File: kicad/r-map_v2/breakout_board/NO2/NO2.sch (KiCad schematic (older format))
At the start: 9 parts

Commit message: Update of schematic and new modules
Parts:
- removed P?: CONN_01X04, symbol CONN_01X04
- removed U?: MICS-2714, symbol MICS-2714
- added C2: 10n, Capacitors_SMD:C_0805_HandSoldering, symbol C
- added C?: C, symbol C
- added P1: CONN_01X08, Pin_Headers:Pin_Header_Straight_1x08_Pitch2.54mm, symbol CONN_01X08
- added P2: CONN_01X02, Pin_Headers:Pin_Header_Straight_1x02_Pitch2.54mm, symbol CONN_01X02
- added Q2: 2N7002, TO_SOT_Packages_SMD:SOT-23, symbol 2N7002
- added R10, R11: R, Resistors_SMD:R_0805, symbol R
- added R6: 330, Resistors_SMD:R_0805, symbol R
- added R7: 10K, Resistors_SMD:R_0805, symbol R
- added R8: R82, Resistors_SMD:R_0805, symbol R
- added R9: 820, Resistors_SMD:R_0805, symbol R
- added RV1, RV2: POT, SMD_Packages:POT_SMD, symbol POT
- added U1: MICS-4514, rmap:MICS-4514, symbol MICS-4514
- C1: renamed from C?; footprint (none) -> Capacitors_SMD:C_0805_HandSoldering
- R1, R2, R3, R4, R5: renamed from R?; footprint (none) -> Resistors_SMD:R_0805
- gave numbers to parts that had none: 1
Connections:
- net labels added: A1, VCC, Vref
- wire segments 35 -> 68
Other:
- moved on the sheet: C1, Q1, R1, R2, R3, R4, R5

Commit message: Update of MICS-4514 board not definitive
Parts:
- removed P1: CONN_01X08, Pin_Headers:Pin_Header_Straight_1x08_Pitch2.54mm, symbol CONN_01X08
- removed P2: CONN_01X02, Pin_Headers:Pin_Header_Straight_1x02_Pitch2.54mm, symbol CONN_01X02
- removed RV1, RV2: POT, SMD_Packages:POT_SMD, symbol POT
- added P1, P2: CONN_01X05, symbol CONN_01X05
- added R12: 1M, symbol R
- R10: value R -> 1M; footprint Resistors_SMD:R_0805 -> (none)
- R11: value R -> 100K; footprint Resistors_SMD:R_0805 -> (none)
- R4: value 56R -> 100K; footprint Resistors_SMD:R_0805 -> (none)
- R5, R9: value 820 -> 10K
- gave numbers to parts that had none: 1
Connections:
- net labels added: D1, D2, D3, D4, FET_DRIVE
- net labels removed: VCC, Vref
- wire segments 68 -> 80
- no-connect marks 0 -> 1
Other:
- moved on the sheet: C1, Q1, R1, R2, R5, R9

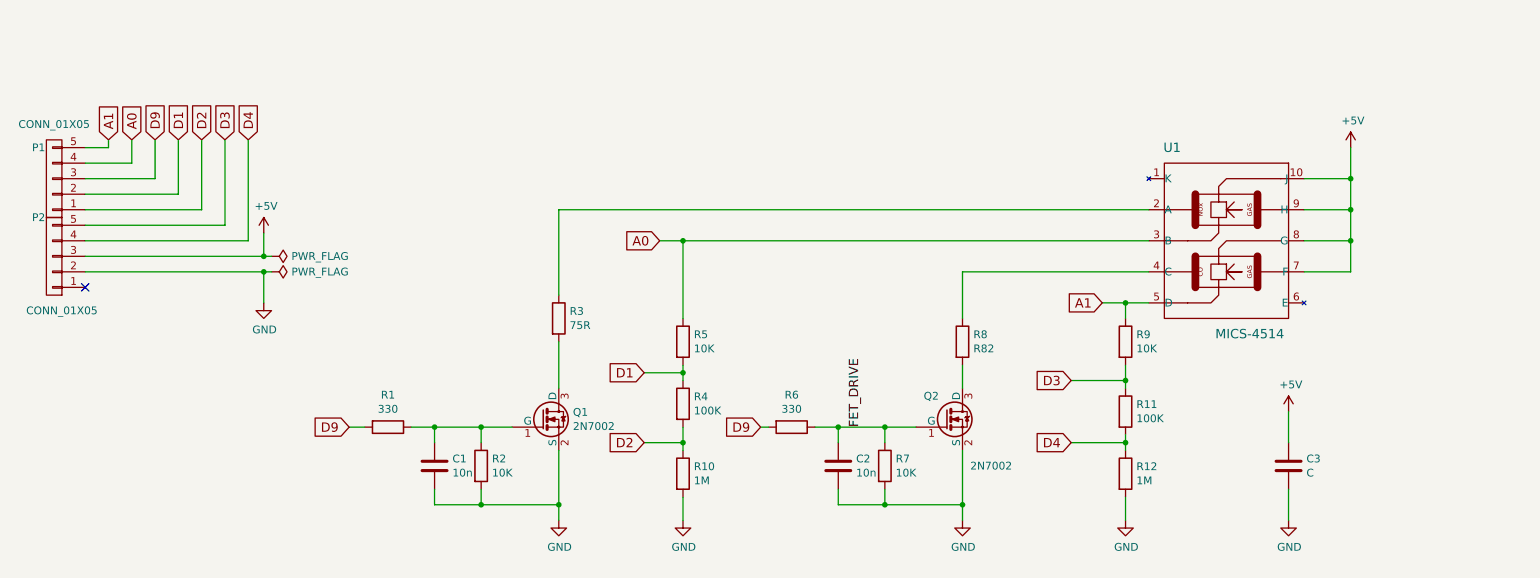
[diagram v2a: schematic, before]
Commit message: Change of label and digital pin assignement on NO2 schematic
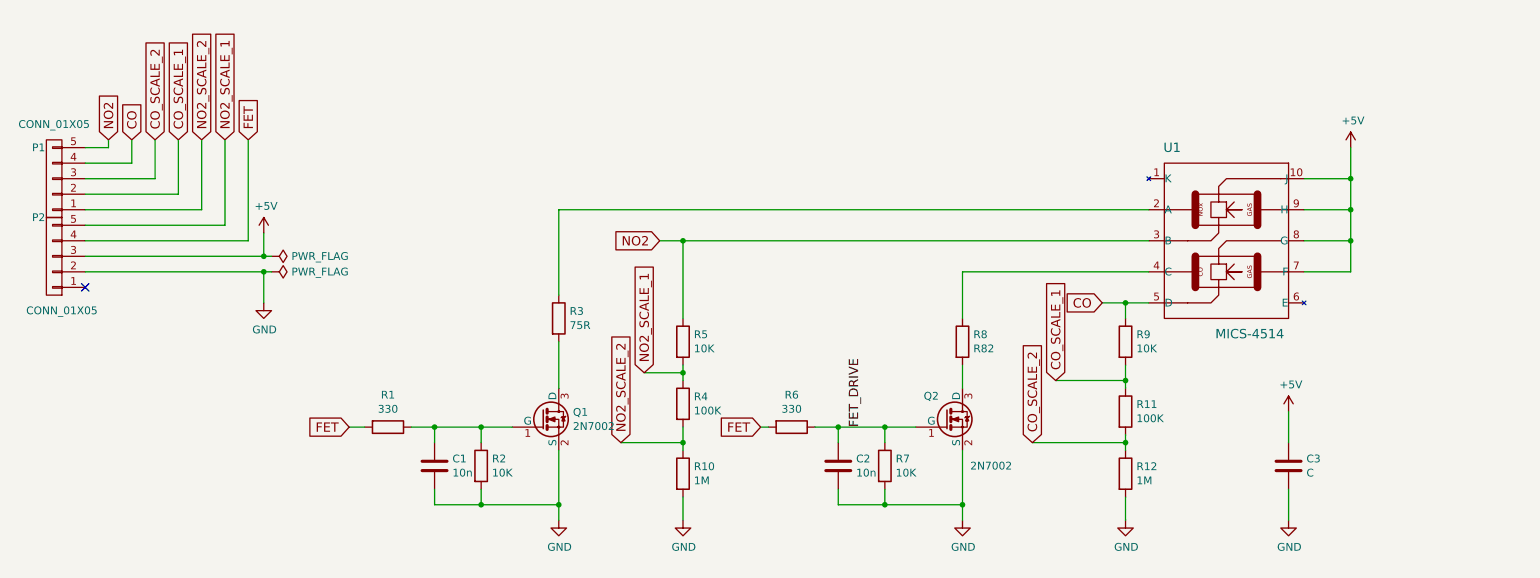
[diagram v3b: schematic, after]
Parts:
- C3: footprint (none) -> Capacitors_SMD:C_0805_HandSoldering
- P1, P2: footprint (none) -> Pin_Headers:Pin_Header_Straight_1x05_Pitch2.54mm
- R1, R2, R3, R5, R6, R7, R8, R9: footprint Resistors_SMD:R_0805 -> Resistors_SMD:R_0805_HandSoldering
- R10, R11, R12, R4: footprint (none) -> Resistors_SMD:R_0805_HandSoldering
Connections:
- net A0 renamed NO2
- net NO2: now also P1.5 (P5); no longer P1.4 (P4)
- net A1 renamed CO
- net CO: now also P1.4 (P4); no longer P1.5 (P5)
- net D1 renamed NO2_SCALE_1
- net NO2_SCALE_1: now also P2.5 (P5); no longer P1.2 (P2)
- net D2 renamed NO2_SCALE_2
- net D3 renamed CO_SCALE_1
- net CO_SCALE_1: now also P1.2 (P2); no longer P2.5 (P5)
- net D4 renamed CO_SCALE_2
- net CO_SCALE_2: now also P1.3 (P3); no longer P2.4 (P4)
- net D9 renamed FET
- net FET: now also P2.4 (P4); no longer P1.3 (P3)
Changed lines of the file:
@@
 F 0 "R3" H 4470 3746 50  0000 L CNN
 F 1 "75R" H 4470 3655 50  0000 L CNN
-F 2 "Resistors_SMD:R_0805" V -670 1050 50  0001 C CNN
+F 2 "Resistors_SMD:R_0805_HandSoldering" V -670 1050 50  0001 C CNN
 F 3 "" H -600 1050 50  0001 C CNN
 	1    4400 3700
@@
 $EndComp
 Wire Wire Line
-	4400 4550 4400 4900
-Wire Wire Line
-	4400 4900 4400 5000
+	4400 4550 4400 5000
 $Comp
 L R R5
@@
 F 0 "R5" H 5270 3896 50  0000 L CNN
 F 1 "10K" H 5270 3805 50  0000 L CNN
-F 2 "Resistors_SMD:R_0805" V 430 850 50  0001 C CNN
+F 2 "Resistors_SMD:R_0805_HandSoldering" V 430 850 50  0001 C CNN
 F 3 "" H 500 850 50  0001 C CNN
 	1    5200 3850
@@
 $EndComp
 Wire Wire Line
-	5200 4000 5200 4050
-Wire Wire Line
-	5200 4050 5200 4100
-Wire Wire Line
-	5200 4400 5200 4500
-Wire Wire Line
-	5200 4500 5200 4550
+	5200 4000 5200 4100
+Wire Wire Line
+	5200 4400 5200 4550
 $Comp
 L R R1
@@
 F 0 "R1" V 3093 4400 50  0000 C CNN
 F 1 "330" V 3184 4400 50  0000 C CNN
-F 2 "Resistors_SMD:R_0805" V 30  700 50  0001 C CNN
+F 2 "Resistors_SMD:R_0805_HandSoldering" V 30  700 50  0001 C CNN
 F 3 "" H 100 700 50  0001 C CNN
 	1    3300 4400
@@
 F 0 "R2" H 3970 4696 50  0000 L CNN
 F 1 "10K" H 3970 4605 50  0000 L CNN
-F 2 "Resistors_SMD:R_0805" V 430 950 50  0001 C CNN
+F 2 "Resistors_SMD:R_0805_HandSoldering" V 430 950 50  0001 C CNN
 F 3 "" H 500 950 50  0001 C CNN
 	1    3900 4650
@@
 	3050 4400 3150 4400
 Wire Wire Line
-	3450 4400 3600 4400
-Wire Wire Line
-	3600 4400 3900 4400
-Wire Wire Line
-	3900 4400 4100 4400
+	3450 4400 4100 4400
 Wire Wire Line
 	3600 4500 3600 4400
@@
 $EndComp
 Wire Wire Line
-	1350 3400 2500 3400
-Wire Wire Line
-	2500 3400 2550 3400
+	1350 3400 2550 3400
 Wire Wire Line
 	2500 3400 2500 3600
@@
 $EndComp
 Wire Wire Line
-	1350 3300 2500 3300
-Wire Wire Line
-	2500 3300 2550 3300
-Wire Wire Line
-	9500 2600 9500 2800
-Wire Wire Line
-	9500 2800 9500 3000
-Wire Wire Line
-	9500 3000 9500 3200
-Wire Wire Line
-	9500 3200 9500 3400
+	1350 3300 2550 3300
+Wire Wire Line
+	9500 2600 9500 3400
 Wire Wire Line
 	9200 2800 9500 2800
@@
 $EndComp
 Wire Wire Line
-	3600 4900 3900 4900
-Wire Wire Line
-	3900 4900 4400 4900
+	3600 4900 4400 4900
 Text GLabel 5050 3200 0    60   Input ~ 0
-A0
+NO2
 Text GLabel 3050 4400 0    60   Input ~ 0
-D9
+FET
 Text GLabel 1800 2550 1    60   Input ~ 0
-D9
+CO_SCALE_2
 Text GLabel 1650 2550 1    60   Input ~ 0
-A0
+CO
 Wire Wire Line
 	1650 2550 1650 2700
@@
 F 0 "R8" H 7070 3896 50  0000 L CNN
 F 1 "R82" H 7070 3805 50  0000 L CNN
-F 2 "Resistors_SMD:R_0805" V -670 -350 50  0001 C CNN
+F 2 "Resistors_SMD:R_0805_HandSoldering" V -670 -350 50  0001 C CNN
 F 3 "" H -600 -350 50  0001 C CNN
 	1    7000 3850
@@
 F 0 "R9" H 8120 3896 50  0000 L CNN
 F 1 "10K" H 8120 3805 50  0000 L CNN
-F 2 "Resistors_SMD:R_0805" V 3280 850 50  0001 C CNN
+F 2 "Resistors_SMD:R_0805_HandSoldering" V 3280 850 50  0001 C CNN
 F 3 "" H 3350 850 50  0001 C CNN
 	1    8050 3850
@@
 $EndComp
 Wire Wire Line
-	7900 3600 8050 3600
-Wire Wire Line
-	8050 3600 8200 3600
+	7900 3600 8200 3600
 Wire Wire Line
 	8050 3600 8050 3700
@@
 Connection ~ 8050 3600
 Text GLabel 7900 3600 0    60   Input ~ 0
-A1
+CO
 Wire Wire Line
 	8050 4850 8050 5000
 Text GLabel 1500 2550 1    60   Input ~ 0
-A1
+NO2
 Wire Wire Line
 	1500 2550 1500 2600
@@
 $EndComp
 Wire Wire Line
-	7000 4550 7000 4900
-Wire Wire Line
-	7000 4900 7000 5000
+	7000 4550 7000 5000
 $Comp
 L R R6
@@
 F 0 "R6" V 5693 4400 50  0000 C CNN
 F 1 "330" V 5784 4400 50  0000 C CNN
-F 2 "Resistors_SMD:R_0805" V 2630 700 50  0001 C CNN
+F 2 "Resistors_SMD:R_0805_HandSoldering" V 2630 700 50  0001 C CNN
 F 3 "" H 2700 700 50  0001 C CNN
 	1    5900 4400
@@
 F 0 "R7" H 6570 4696 50  0000 L CNN
 F 1 "10K" H 6570 4605 50  0000 L CNN
-F 2 "Resistors_SMD:R_0805" V 3030 950 50  0001 C CNN
+F 2 "Resistors_SMD:R_0805_HandSoldering" V 3030 950 50  0001 C CNN
 F 3 "" H 3100 950 50  0001 C CNN
 	1    6500 4650
@@
 	5700 4400 5750 4400
 Wire Wire Line
-	6050 4400 6200 4400
-Wire Wire Line
-	6200 4400 6500 4400
-Wire Wire Line
-	6500 4400 6700 4400
+	6050 4400 6700 4400
 Wire Wire Line
 	6200 4500 6200 4400
@@
 Connection ~ 6500 4900
 Wire Wire Line
-	6200 4900 6500 4900
-Wire Wire Line
-	6500 4900 7000 4900
+	6200 4900 7000 4900
 Text GLabel 5700 4400 0    60   Input ~ 0
-D9
+FET
 Wire Wire Line
 	4400 3000 4400 3550
 Wire Wire Line
-	5050 3200 5200 3200
-Wire Wire Line
-	5200 3200 8200 3200
+	5050 3200 8200 3200
 Wire Wire Line
 	4400 3000 8200 3000
@@
 F 0 "C3" H 9215 4696 50  0000 L CNN
 F 1 "C" H 9215 4605 50  0000 L CNN
-F 2 "" H 188 0   50  0001 C CNN
+F 2 "Capacitors_SMD:C_0805_HandSoldering" H 188 0   50  0001 C CNN
 F 3 "" H 150 150 50  0001 C CNN
 	1    9100 4650
@@
 F 0 "R12" H 8120 4746 50  0000 L CNN
 F 1 "1M" H 8120 4655 50  0000 L CNN
-F 2 "" V -20 -50 50  0001 C CNN
+F 2 "Resistors_SMD:R_0805_HandSoldering" V -20 -50 50  0001 C CNN
 F 3 "" H 50  -50 50  0001 C CNN
 	1    8050 4700
@@
 F 0 "R10" H 5270 4746 50  0000 L CNN
 F 1 "1M" H 5270 4655 50  0000 L CNN
-F 2 "" V -70 50  50  0001 C CNN
+F 2 "Resistors_SMD:R_0805_HandSoldering" V -70 50  50  0001 C CNN
 F 3 "" H 0   50  50  0001 C CNN
 	1    5200 4700
@@
 F 0 "R4" H 5270 4296 50  0000 L CNN
 F 1 "100K" H 5270 4205 50  0000 L CNN
-F 2 "" V -70 0   50  0001 C CNN
+F 2 "Resistors_SMD:R_0805_HandSoldering" V -70 0   50  0001 C CNN
 F 3 "" H 0   0   50  0001 C CNN
 	1    5200 4250
@@
 F 0 "R11" H 8120 4346 50  0000 L CNN
 F 1 "100K" H 8120 4255 50  0000 L CNN
-F 2 "" V 2780 50  50  0001 C CNN
+F 2 "Resistors_SMD:R_0805_HandSoldering" V 2780 50  50  0001 C CNN
 F 3 "" H 2850 50  50  0001 C CNN
 	1    8050 4300
@@
 $EndComp
 Wire Wire Line
-	8050 4000 8050 4100
-Wire Wire Line
-	8050 4100 8050 4150
-Wire Wire Line
-	8050 4450 8050 4500
-Wire Wire Line
-	8050 4500 8050 4550
-Text GLabel 4950 4050 0    60   Input ~ 0
-D1
+	8050 4000 8050 4150
+Wire Wire Line
+	8050 4450 8050 4550
+Text GLabel 4950 4050 1    60   Input ~ 0
+NO2_SCALE_1
 Wire Wire Line
 	4950 4050 5200 4050
 Connection ~ 5200 4050
-Text GLabel 4950 4500 0    60   Input ~ 0
-D2
-Wire Wire Line
-	4950 4500 5200 4500
+Text GLabel 4800 4500 1    60   Input ~ 0
+NO2_SCALE_2
+Wire Wire Line
+	4800 4500 5200 4500
 Connection ~ 5200 4500
-Text GLabel 7700 4100 0    60   Input ~ 0
-D3
-Wire Wire Line
-	7700 4100 8050 4100
+Text GLabel 7600 4100 1    60   Input ~ 0
+CO_SCALE_1
+Wire Wire Line
+	7600 4100 8050 4100
 Connection ~ 8050 4100
-Text GLabel 7700 4500 0    60   Input ~ 0
-D4
-Wire Wire Line
-	7700 4500 8050 4500
+Text GLabel 7450 4500 1    60   Input ~ 0
+CO_SCALE_2
+Wire Wire Line
+	7450 4500 8050 4500
 Connection ~ 8050 4500
 Text GLabel 1950 2550 1    60   Input ~ 0
-D1
+CO_SCALE_1
 Text GLabel 2100 2550 1    60   Input ~ 0
-D2
+NO2_SCALE_2
 Text GLabel 2250 2550 1    60   Input ~ 0
-D3
+NO2_SCALE_1
 Text GLabel 2400 2550 1    60   Input ~ 0
-D4
+FET
 Wire Wire Line
 	1950 2550 1950 2900
@@
 F 0 "P1" H 1250 2600 50  0000 C CNN
 F 1 "CONN_01X05" H 1150 2450 50  0000 C CNN
-F 2 "" H 0   -150 50  0001 C CNN
+F 2 "Pin_Headers:Pin_Header_Straight_1x05_Pitch2.54mm" H 0   -150 50  0001 C CNN
 F 3 "" H 0   -150 50  0001 C CNN
 	1    1150 2800
@@
 F 0 "P2" H 1250 3050 50  0000 C CNN
 F 1 "CONN_01X05" H 1100 3650 50  0000 C CNN
-F 2 "" H 0   100 50  0001 C CNN
+F 2 "Pin_Headers:Pin_Header_Straight_1x05_Pitch2.54mm" H 0   100 50  0001 C CNN
 F 3 "" H 0   100 50  0001 C CNN
 	1    1150 3300
